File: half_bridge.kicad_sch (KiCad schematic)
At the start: 23 parts, among them Q1 IGC025S08S1, Q2 IGC025S08S1, U4 AD8418, U5 LMG1205YFXR, U6 SN74LVC1G66DCKR

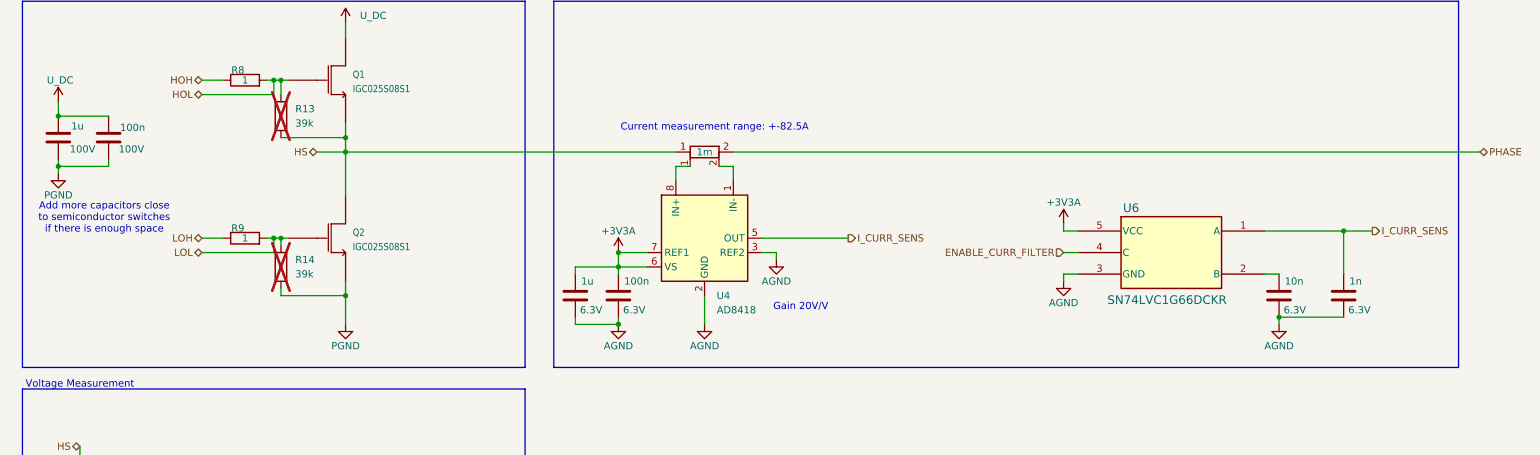
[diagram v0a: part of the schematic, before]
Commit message: Analog current filters were removed, some footprints were fixed and initial rough layout has been made.
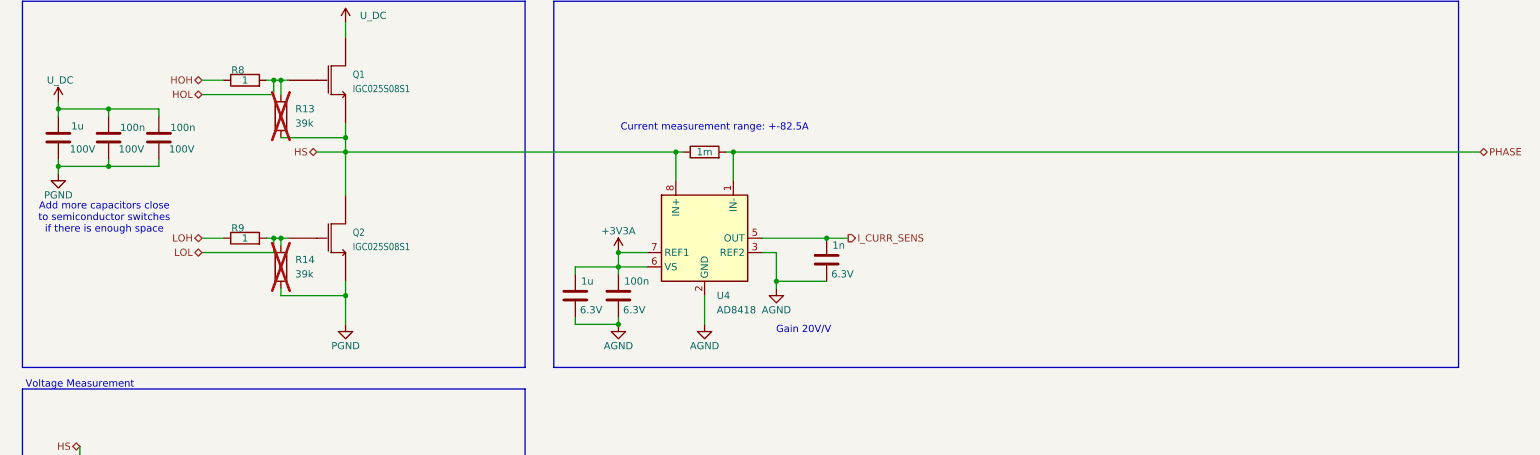
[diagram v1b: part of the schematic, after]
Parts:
- removed C27: 10n, Capacitor_SMD:C_0201_0603Metric, symbol Device:C
- removed R11: 1m, NanoGaN:RES_00FEA_VIS-L, symbol NanoGaN:WSLF25121L000FEA
- removed U6: SN74LVC1G66DCKR, NanoGaN:DCK5, symbol NanoGaN:SN74LVC1G66DCKR
- added C15: 100n, Capacitor_SMD:C_0805_2012Metric, symbol Device:C
- added R11: 1m, NanoGaN:RES_00FEA_VIS-L, symbol Device:R
- R13, R14: footprint Resistor_SMD:R_0402_1005Metric_Pad0.72x0.64mm_HandSolder -> Resistor_SMD:R_0402_1005Metric
- R8, R9: footprint Resistor_SMD:R_0508_1220Metric_Pad1.12x2.15mm_HandSolder -> Resistor_SMD:R_0402_1005Metric; LCSC C510151 -> C2077491
- U4: footprint (none) -> Package_SO:SOIC-8_3.9x4.9mm_P1.27mm
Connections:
- net HOL: now also Q1.1 (G); no longer Q1.3 (G)
- net HS: now also Q1.3 (S1), Q2.4 (D1), U4.8 (IN+), R11.1; no longer Q1.4 (S1), Q2.1 (D1)
- net LOL: now also Q2.1 (G); no longer Q2.3 (G)
- net PGND: now also Q2.3 (S1), C15.2; no longer Q2.4 (S1)
- net PHASE: now also U4.1 (IN-), R11.2
- net U_DC: now also Q1.4 (D1), C15.1; no longer Q1.1 (D1)

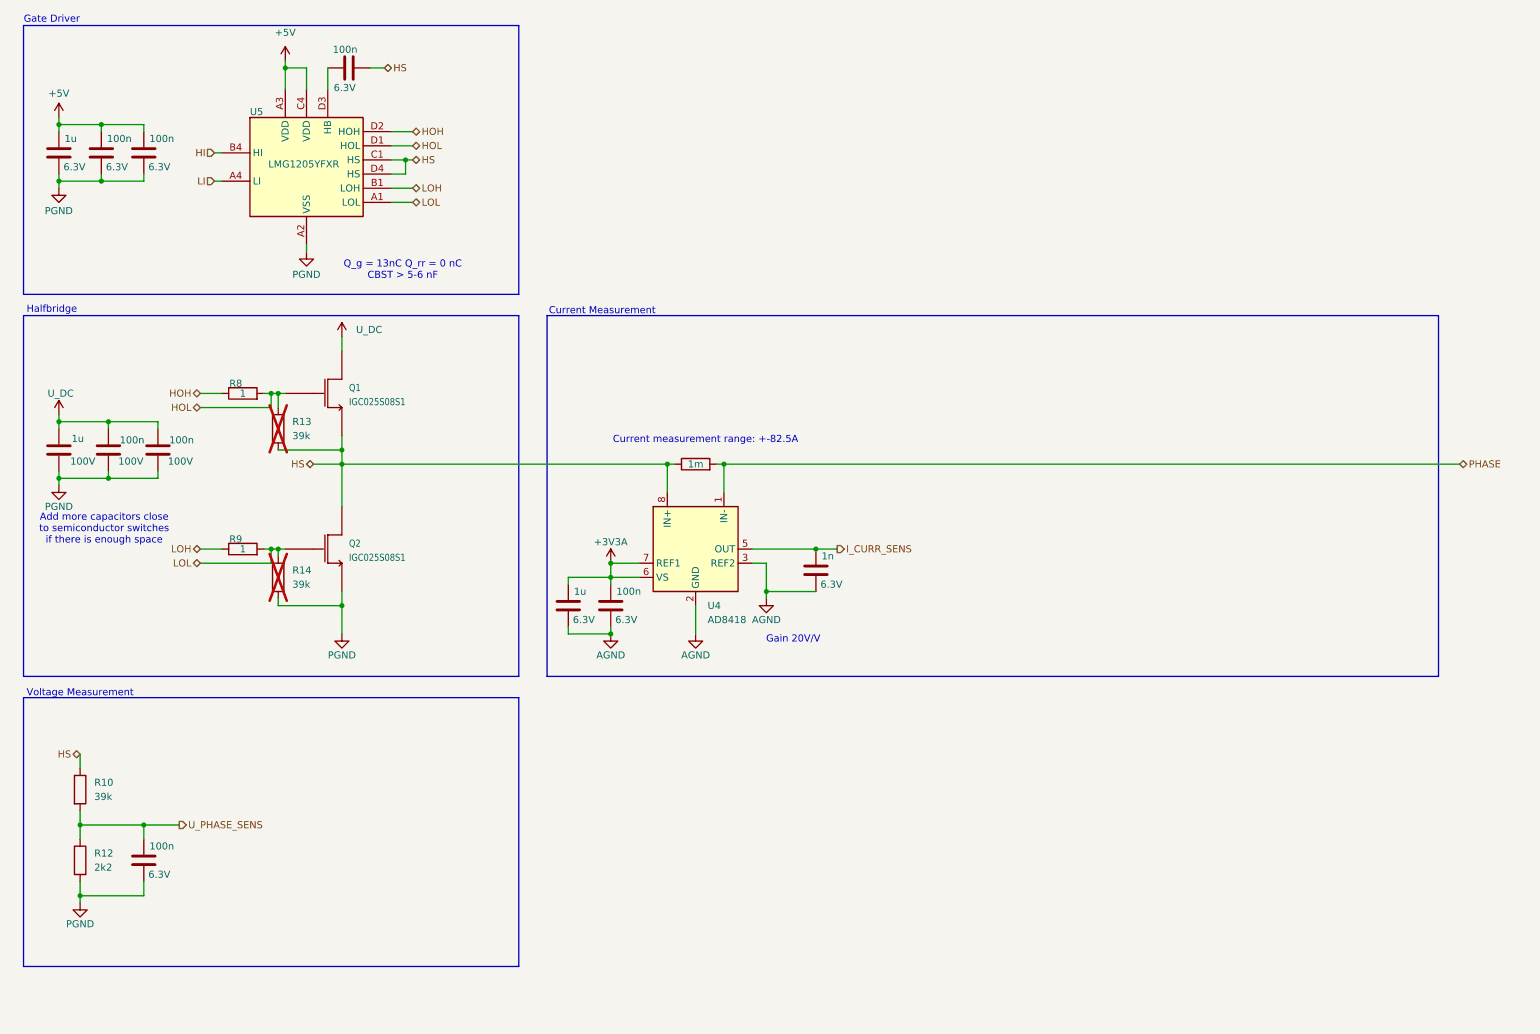
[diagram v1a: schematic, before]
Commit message: pdf export and small fixes
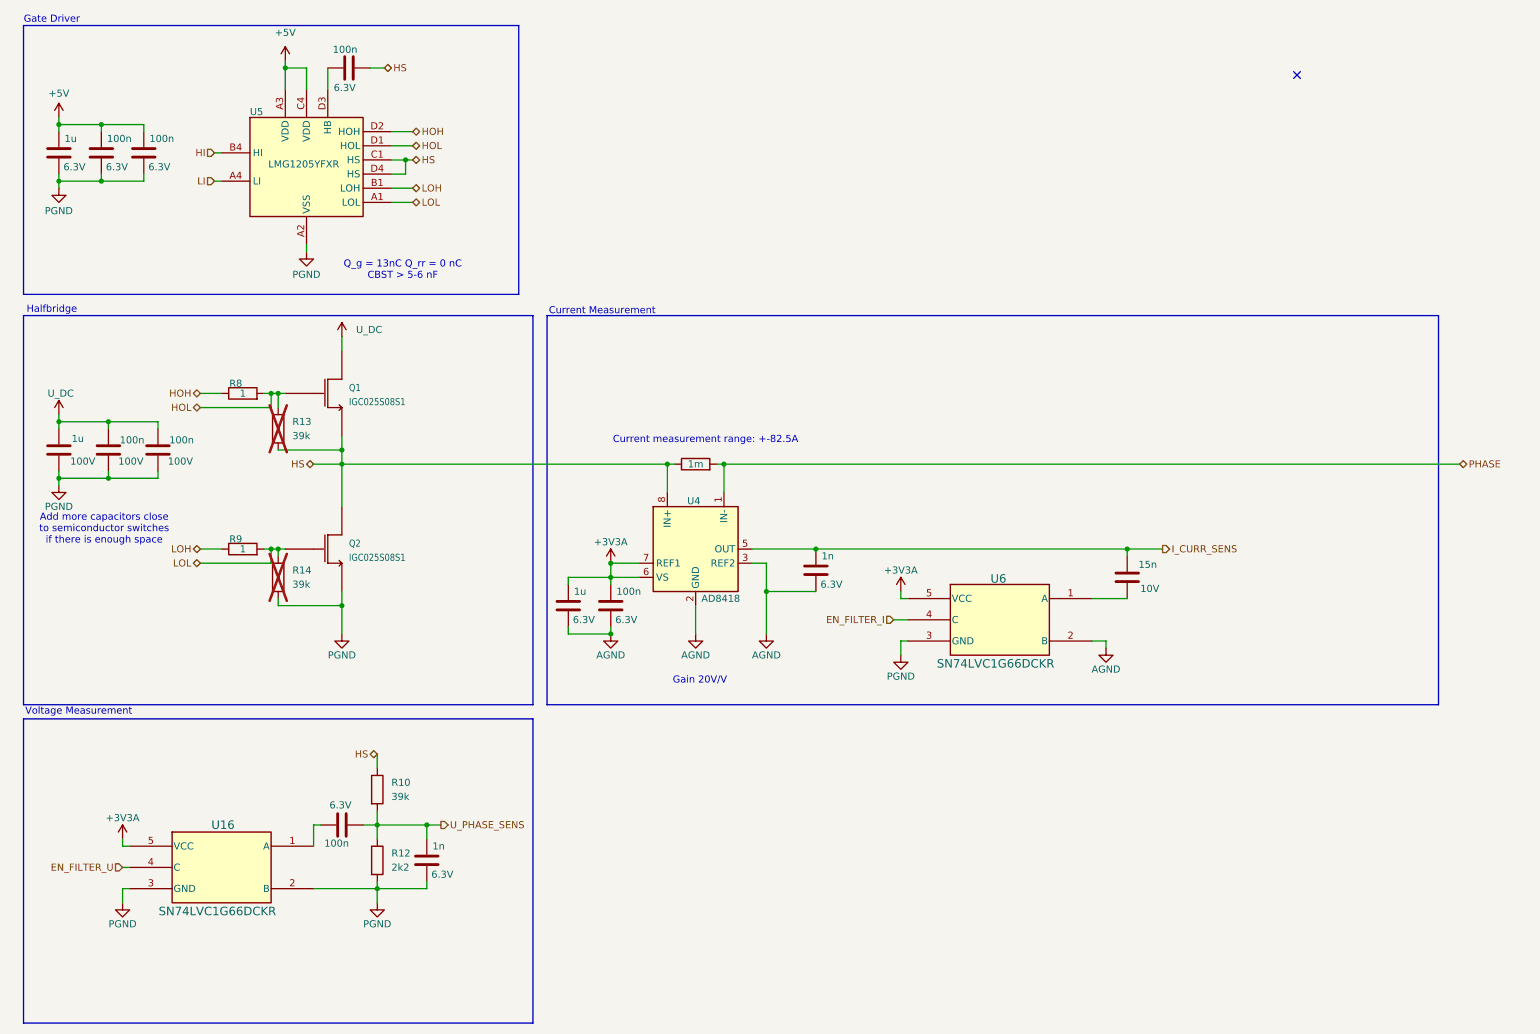
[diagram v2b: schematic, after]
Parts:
- added C87: 1n, Capacitor_SMD:C_0201_0603Metric, symbol Device:C
- added C90: 15n, Capacitor_SMD:C_0402_1005Metric, symbol Device:C
- added U16, U6: SN74LVC1G66DCKR, NanoGaN:DCK5, symbol NanoGaN:SN74LVC1G66DCKR
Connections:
- net +3V3A: now also U16.5 (VCC), U6.5 (VCC)
- net AGND: now also U6.2 (B)
- net I_CURR_SENS: now also C90.1
- net PGND: now also C87.2, U16.2 (B), U16.3 (GND), U6.3 (GND); no longer C25.2
- net U_PHASE_SENS: now also C25.2, C87.1; no longer C25.1
- new net: C25.1, U16.1 (A)
- new net: C90.2, U6.1 (A)
- new net EN_FILTER_I: U6.4 (C)
- new net EN_FILTER_U: U16.4 (C)
- no-connect marks 0 -> 1
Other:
- moved on the sheet: R10, R12

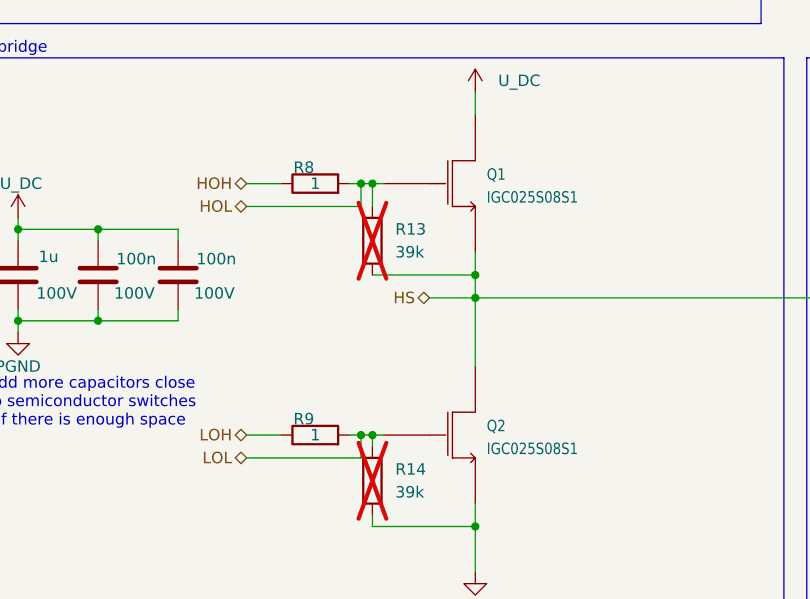
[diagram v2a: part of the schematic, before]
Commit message: Differential pair naming added. Duplicate footprint problem fixed.
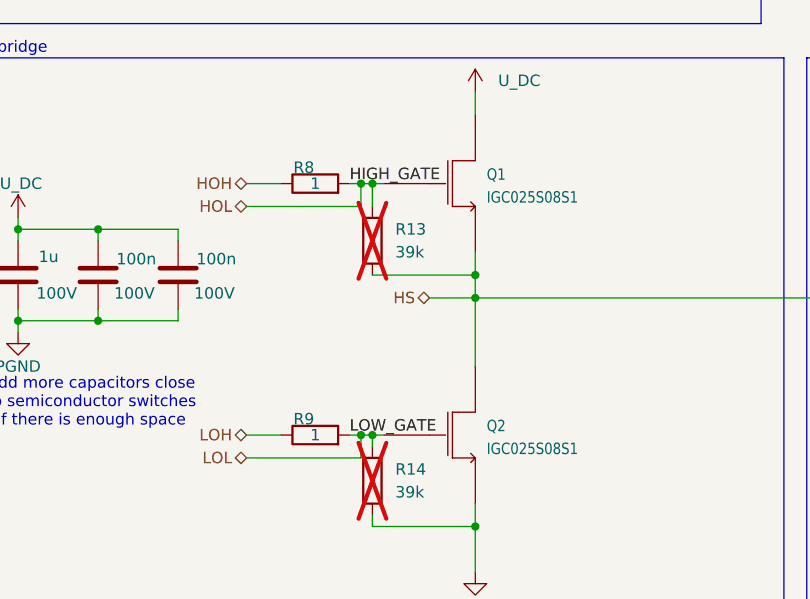
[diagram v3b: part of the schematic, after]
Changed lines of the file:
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@@
+		)
+	)
+	(label "LOW_GATE"
+		(at 55.88 109.22 0)
+		(effects
+			(font
+				(size 1.27 1.27)
+			)
+			(justify left bottom)
+		)
+	)
+	(label "HIGH_GATE"
+		(at 55.88 81.28 0)
+		(effects
+			(font
+				(size 1.27 1.27)
+			)
+			(justify left bottom)
 		)
 	)
